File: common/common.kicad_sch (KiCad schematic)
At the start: 1 part, among them J1 Conn_01x08_Socket

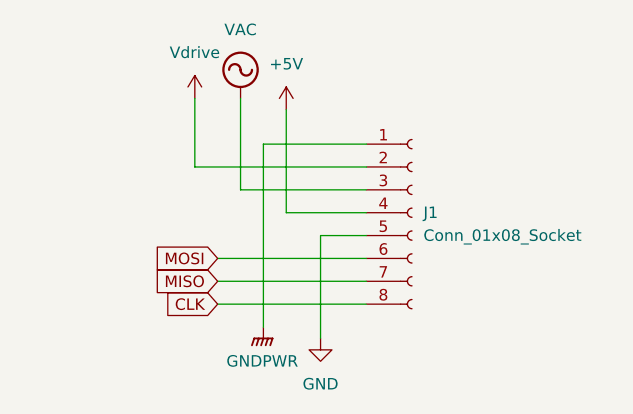
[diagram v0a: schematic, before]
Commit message: expansion schematics added
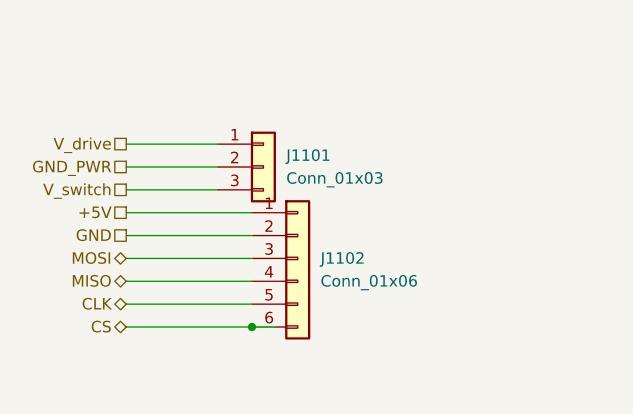
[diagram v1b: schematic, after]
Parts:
- removed J1: Conn_01x08_Socket, TerminalBlock_4Ucon:TerminalBlock_4Ucon_1x08_P3.50mm_Vertical, symbol Connector:Conn_01x08_Socket
- added J1101: Conn_01x03, TerminalBlock_4Ucon:TerminalBlock_4Ucon_1x03_P3.50mm_Vertical, symbol Connector_Generic:Conn_01x03
- added J1102: Conn_01x06, TerminalBlock_4Ucon:TerminalBlock_4Ucon_1x06_P3.50mm_Vertical, symbol Connector_Generic:Conn_01x06
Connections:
- net +5V: now also J1102.1 (Pin_1)
- net CLK: now also J1102.5 (Pin_5)
- net GND: now also J1102.2 (Pin_2)
- net MISO: now also J1102.4 (Pin_4)
- net MOSI: now also J1102.3 (Pin_3)
- new net CS: J1102.6 (Pin_6)
- new net GND_PWR: J1101.2 (Pin_2)
- new net V_drive: J1101.1 (Pin_1)
- new net V_switch: J1101.3 (Pin_3)

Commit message: Finalise expansion A.
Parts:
- renumbered J1101 to J201, J1102 to J202
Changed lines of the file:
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@@
 		(dnp no)
 		(fields_autoplaced yes)
-		(property "Reference" "J1102"
+		(property "Reference" "J202"
 			(at 44.45 45.7199 0)
 			(effects
@@
 		(dnp no)
 		(fields_autoplaced yes)
-		(property "Reference" "J1101"
+		(property "Reference" "J201"
 			(at 40.64 34.2899 0)
 			(effects

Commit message: Expander Final II
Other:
- company: (none) -> Jens Böckmann
- title: (none) -> Default Adapter
- moved on the sheet: J201, J202
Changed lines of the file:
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@@
 	(generator_version "8.0")
 	(paper "A4")
+	(title_block
+		(title "Default Adapter")
+		(date "2025-01-01")
+		(rev "1")
+		(company "Jens Böckmann")
+	)
 	(junction
-		(at 36.83 53.34)
+		(at 157.48 110.49)
 		(diameter 0)
 		(color 0 0 0 0)
@@
 	(wire
 		(pts
-			(xy 22.86 33.02) (xy 33.02 33.02)
-		)
-		(stroke
-			(width 0)
-			(type default)
-		)
-	)
-	(wire
-		(pts
-			(xy 22.86 35.56) (xy 33.02 35.56)
-		)
-		(stroke
-			(width 0)
-			(type default)
-		)
-	)
-	(wire
-		(pts
-			(xy 22.86 40.64) (xy 36.83 40.64)
-		)
-		(stroke
-			(width 0)
-			(type default)
-		)
-	)
-	(wire
-		(pts
-			(xy 22.86 45.72) (xy 36.83 45.72)
-		)
-		(stroke
-			(width 0)
-			(type default)
-		)
-	)
-	(wire
-		(pts
-			(xy 22.86 48.26) (xy 36.83 48.26)
-		)
-		(stroke
-			(width 0)
-			(type default)
-		)
-	)
-	(wire
-		(pts
-			(xy 22.86 53.34) (xy 36.83 53.34)
-		)
-		(stroke
-			(width 0)
-			(type default)
-		)
-	)
-	(wire
-		(pts
-			(xy 22.86 43.18) (xy 36.83 43.18)
-		)
-		(stroke
-			(width 0)
-			(type default)
-		)
-	)
-	(wire
-		(pts
-			(xy 22.86 50.8) (xy 36.83 50.8)
-		)
-		(stroke
-			(width 0)
-			(type default)
-		)
-	)
-	(wire
-		(pts
-			(xy 36.83 53.34) (xy 39.37 53.34)
-		)
-		(stroke
-			(width 0)
-			(type default)
-		)
-	)
-	(wire
-		(pts
-			(xy 22.86 38.1) (xy 33.02 38.1)
+			(xy 143.51 90.17) (xy 153.67 90.17)
+		)
+		(stroke
+			(width 0)
+			(type default)
+		)
+	)
+	(wire
+		(pts
+			(xy 143.51 92.71) (xy 153.67 92.71)
+		)
+		(stroke
+			(width 0)
+			(type default)
+		)
+	)
+	(wire
+		(pts
+			(xy 143.51 97.79) (xy 157.48 97.79)
+		)
+		(stroke
+			(width 0)
+			(type default)
+		)
+	)
+	(wire
+		(pts
+			(xy 143.51 102.87) (xy 157.48 102.87)
+		)
+		(stroke
+			(width 0)
+			(type default)
+		)
+	)
+	(wire
+		(pts
+			(xy 143.51 105.41) (xy 157.48 105.41)
+		)
+		(stroke
+			(width 0)
+			(type default)
+		)
+	)
+	(wire
+		(pts
+			(xy 143.51 110.49) (xy 157.48 110.49)
+		)
+		(stroke
+			(width 0)
+			(type default)
+		)
+	)
+	(wire
+		(pts
+			(xy 143.51 100.33) (xy 157.48 100.33)
+		)
+		(stroke
+			(width 0)
+			(type default)
+		)
+	)
+	(wire
+		(pts
+			(xy 143.51 107.95) (xy 157.48 107.95)
+		)
+		(stroke
+			(width 0)
+			(type default)
+		)
+	)
+	(wire
+		(pts
+			(xy 157.48 110.49) (xy 160.02 110.49)
+		)
+		(stroke
+			(width 0)
+			(type default)
+		)
+	)
+	(wire
+		(pts
+			(xy 143.51 95.25) (xy 153.67 95.25)
 		)
 		(stroke
@@
 	(hierarchical_label "V_switch"
 		(shape passive)
-		(at 22.86 38.1 180)
+		(at 143.51 95.25 180)
 		(fields_autoplaced yes)
 		(effects
@@
 	(hierarchical_label "GND"
 		(shape passive)
-		(at 22.86 43.18 180)
+		(at 143.51 100.33 180)
 		(fields_autoplaced yes)
 		(effects
@@
 	(hierarchical_label "V_drive"
 		(shape passive)
-		(at 22.86 33.02 180)
+		(at 143.51 90.17 180)
 		(fields_autoplaced yes)
 		(effects
@@
 	(hierarchical_label "CS"
 		(shape bidirectional)
-		(at 22.86 53.34 180)
+		(at 143.51 110.49 180)
 		(fields_autoplaced yes)
 		(effects
@@
 	(hierarchical_label "+5V"
 		(shape passive)
-		(at 22.86 40.64 180)
+		(at 143.51 97.79 180)
 		(fields_autoplaced yes)
 		(effects
@@
 	(hierarchical_label "MISO"
 		(shape bidirectional)
-		(at 22.86 48.26 180)
+		(at 143.51 105.41 180)
 		(fields_autoplaced yes)
 		(effects
@@
 	(hierarchical_label "GND_PWR"
 		(shape passive)
-		(at 22.86 35.56 180)
+		(at 143.51 92.71 180)
 		(fields_autoplaced yes)
 		(effects
@@
 	(hierarchical_label "CLK"
 		(shape bidirectional)
-		(at 22.86 50.8 180)
+		(at 143.51 107.95 180)
 		(fields_autoplaced yes)
 		(effects
@@
 	(hierarchical_label "MOSI"
 		(shape bidirectional)
-		(at 22.86 45.72 180)
+		(at 143.51 102.87 180)
 		(fields_autoplaced yes)
 		(effects
@@
 	(symbol
 		(lib_id "Connector_Generic:Conn_01x06")
-		(at 41.91 45.72 0)
+		(at 162.56 102.87 0)
 		(unit 1)
 		(exclude_from_sim no)
@@
 		(fields_autoplaced yes)
 		(property "Reference" "J202"
-			(at 44.45 45.7199 0)
+			(at 165.1 102.8699 0)
 			(effects
 				(font
@@
 		)
 		(property "Value" "Conn_01x06"
-			(at 44.45 48.2599 0)
+			(at 165.1 105.4099 0)
 			(effects
 				(font
@@
 		)
 		(property "Footprint" "TerminalBlock_4Ucon:TerminalBlock_4Ucon_1x06_P3.50mm_Vertical"
-			(at 41.91 45.72 0)
+			(at 162.56 102.87 0)
 			(effects
 				(font
@@
 		)
 		(property "Datasheet" "~"
-			(at 41.91 45.72 0)
+			(at 162.56 102.87 0)
 			(effects
 				(font
@@
 		)
 		(property "Description" "Generic connector, single row, 01x06, script generated (kicad-library-utils/schlib/autogen/connector/)"
-			(at 41.91 45.72 0)
+			(at 162.56 102.87 0)
 			(effects
 				(font
@@
 		)
 		(property "LCSC" "C976560"
-			(at 41.91 45.72 0)
+			(at 162.56 102.87 0)
 			(effects
 				(font
@@
 	(symbol
 		(lib_id "Connector_Generic:Conn_01x03")
-		(at 38.1 35.56 0)
+		(at 158.75 92.71 0)
 		(unit 1)
 		(exclude_from_sim no)
@@
 		(fields_autoplaced yes)
 		(property "Reference" "J201"
-			(at 40.64 34.2899 0)
+			(at 161.29 91.4399 0)
 			(effects
 				(font
@@
 		)
 		(property "Value" "Conn_01x03"
-			(at 40.64 36.8299 0)
+			(at 161.29 93.9799 0)
 			(effects
 				(font
@@
 		)
 		(property "Footprint" "TerminalBlock_4Ucon:TerminalBlock_4Ucon_1x03_P3.50mm_Vertical"
-			(at 38.1 35.56 0)
+			(at 158.75 92.71 0)
 			(effects
 				(font
@@
 		)
 		(property "Datasheet" "~"
-			(at 38.1 35.56 0)
+			(at 158.75 92.71 0)
 			(effects
 				(font
@@
 		)
 		(property "Description" "Generic connector, single row, 01x03, script generated (kicad-library-utils/schlib/autogen/connector/)"
-			(at 38.1 35.56 0)
+			(at 158.75 92.71 0)
 			(effects
 				(font
@@
 		)
 		(property "LCSC" "C976557"
-			(at 38.1 35.56 0)
-			(effects
-				(font
+			(at 158.75 92.71 0)
+			(effects
+				(font

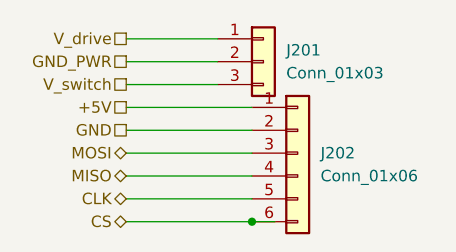
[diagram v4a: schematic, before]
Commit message: Rename common "+5V" to "3V3"
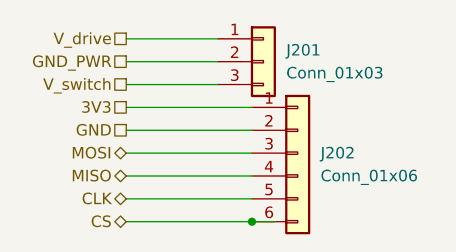
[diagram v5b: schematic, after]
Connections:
- net +5V renamed 3V3
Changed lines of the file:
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@@
 		)
 	)
-	(hierarchical_label "+5V"
+	(hierarchical_label "3V3"
 		(shape passive)
 		(at 143.51 97.79 180)
@@
 				)
 			)
+			(project ""
+				(path "/e63e39d7-6ac0-4ffd-8aa3-1841a4541b55/be4cc6bd-ceea-46b6-92b6-aa36a5c51c8f"
+					(reference "J202")
+					(unit 1)
+				)
+			)
 		)
 	)
@@
 					(unit 1)
 				)
+			)
+			(project ""
+				(path "/e63e39d7-6ac0-4ffd-8aa3-1841a4541b55/be4cc6bd-ceea-46b6-92b6-aa36a5c51c8f"
+					(reference "J201")
+					(unit 1)
+				)
